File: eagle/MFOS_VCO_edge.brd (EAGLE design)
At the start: 99 x 80 mm, 110 parts, among them IC1 TL072P, IC2 LM394N, IC3 TL072P, IC4 TL072P, IC5 TL072P, IC6 TL072P, IC7 LM13700N, U1 2N5457, U2 POWER

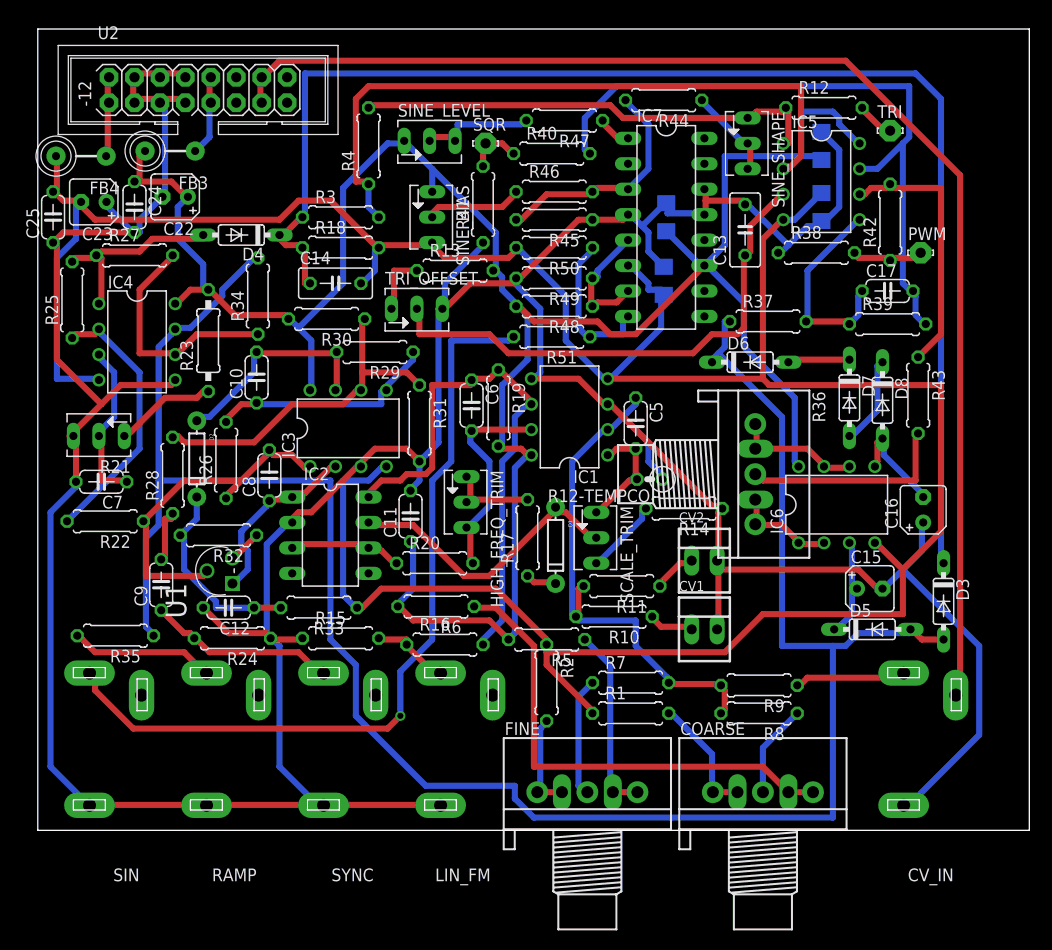
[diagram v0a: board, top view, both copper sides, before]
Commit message: flexible trimmers and grounded air outputs and connector for PWM pot
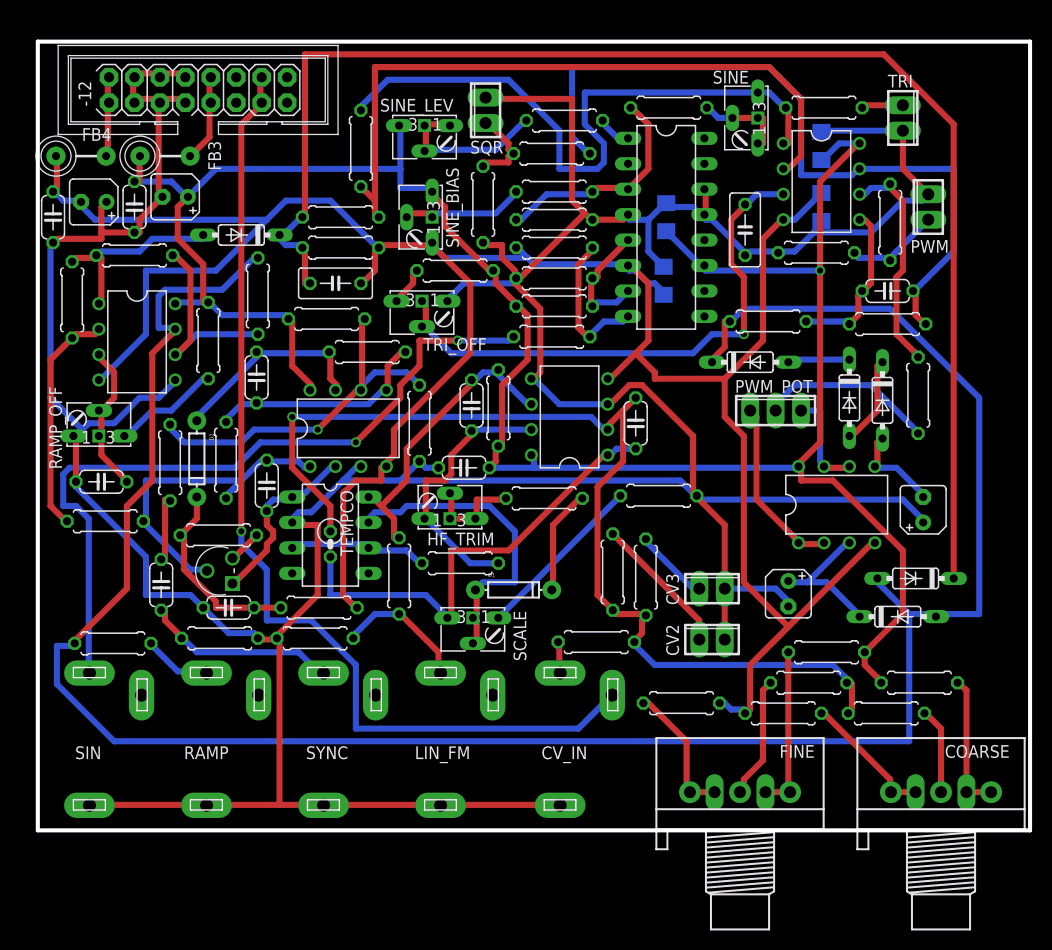
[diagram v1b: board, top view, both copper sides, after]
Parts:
- removed CV1: 22-23-2021, con-molex:22-23-2021
- removed HIGH_FREQ_TRIM, SINE_SHAPE: 100k, pot:B64Y
- removed R12-TEMPCO: 2k, rcl:0207/2V
- removed R21, TRI_OFFSET: 10k, pot:B64Y
- removed R36: 100k, pot:3RP/1610N
- removed SCALE_TRIM: 100R, pot:B64Y
- removed SINE_LEVEL: 1M, pot:B64Y
- added CV3: (no value), con-phoenix-254:2POL254
- added HF_TRIM, SINE: 100k, pot:B64W
- added PWM_POT: 100k, con-phoenix-254:3POL254
- added RAMP_OFF, TRI_OFF: 10k, pot:B64W
- added SCALE: 100R, pot:B64W
- added SINE_LEV: 1M, pot:B64W
- added TEMPCO: 2k, rcl:0207/2V
- C11: value 0.1uF -> 100n
- C8: value .005uF -> 5nF PSA
- C9: value .001uF -> 1n
- CV2: value 22-23-2021 -> (none); device con-molex:22-23-2021 -> con-phoenix-254:2POL254
- PWM, SQR, TRI: value LSP10 -> (none); device solpad:LSP10 -> con-phoenix-254:2POL254
- R23: device rcl:0207/10 -> rcl:0207/7
- SINE_BIAS: device pot:B64Y -> pot:B64W
- moved R6 48.9 mm to (88.0, 14.7)
- moved CV_IN 34.3 mm to (57.1, 0.00)
- moved R5 28.0 mm to (78.7, 17.8), turned to 0 degrees
- moved COARSE 17.8 mm to (90.2, 3.81)
- moved R7 17.8 mm to (77.0, 14.7)
- moved R9 16.8 mm to (55.8, 18.8), turned to 0 degrees
- moved FINE 15.2 mm to (70.1, 3.81)
- moved R1 15.2 mm to (74.4, 11.7)
- moved R2 13.6 mm to (64.3, 12.7), turned to 180 degrees
- moved R8 12.7 mm to (84.7, 11.7)
- moved R16 8.24 mm to (36.1, 25.4), turned to 90 degrees
- moved C15 8.14 mm to (74.9, 23.6), turned to 270 degrees
- moved CV2 7.91 mm to (67.3, 19.1)
- moved C11 7.19 mm to (42.5, 36.2), turned to 180 degrees
- moved D1 6.11 mm to (47.5, 24.0), turned to 0 degrees
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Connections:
- net +12V: now also SINE_LEV.E; no longer SINE_LEVEL.E
- net GND: now also CV3.2, PWM.2, RAMP_OFF.A, SQR.2, TRI.2, TRI_OFF.A; no longer CV1.2, R21.A, TRI_OFFSET.A
- net N$10: now also TEMPCO.1; no longer R12-TEMPCO.1
- net N$14: now also HF_TRIM.E, HF_TRIM.P$1, HF_TRIM.S; no longer HIGH_FREQ_TRIM.E, HIGH_FREQ_TRIM.S
- net N$16: now also HF_TRIM.A; no longer HIGH_FREQ_TRIM.A
- net N$18: now also CV2.1; no longer CV1.1
- net N$19: now also CV3.1; no longer CV2.1
- net N$27: now also RAMP_OFF.E; no longer R21.E
- net N$28: now also RAMP_OFF.P$1, RAMP_OFF.S; no longer R21.S
- net N$46: now also SINE.E; no longer SINE_SHAPE.E
- net N$47: now also TRI.1; no longer TRI.MP
- net N$48: now also TRI_OFF.E; no longer TRI_OFFSET.E
- net N$49: now also TRI_OFF.P$1, TRI_OFF.S; no longer TRI_OFFSET.S
- net N$52: now also PWM_POT.1; no longer R36.3, R36.6
- net N$53: now also PWM_POT.3; no longer R36.1, R36.4
- net N$54: now also PWM.1; no longer PWM.MP
- net N$57: now also SQR.1; no longer SQR.MP
- net N$59: now also PWM_POT.2; no longer R36.2
- net N$60: now also SINE.A, SINE.P$1, SINE.S; no longer SINE_SHAPE.A, SINE_SHAPE.S
- net N$62: now also SINE_BIAS.P$1
- net N$64: now also SINE_LEV.A, SINE_LEV.P$1, SINE_LEV.S; no longer SINE_LEVEL.A, SINE_LEVEL.S
- net N$7: now also SCALE.A; no longer SCALE_TRIM.A
- net N$8: now also SCALE.P$1, SCALE.S; no longer SCALE_TRIM.S
- net N$9: now also SCALE.E, TEMPCO.2; no longer R12-TEMPCO.2, SCALE_TRIM.E
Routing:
- net N$10: track 58.4 -> 104.5 mm, vias 0 -> 1
- net -12V: track 286.0 -> 250.8 mm
- net N$4: track 48.6 -> 13.8 mm
- net N$9: track 11.6 -> 46.0 mm
- net N$13: track 129.8 -> 100.2 mm, vias 0 -> 1
- net GND: track 408.6 -> 433.1 mm
- net N$40: track 54.8 -> 30.6 mm
- net N$46: track 47.0 -> 64.5 mm
- net N$35: track 209.3 -> 225.5 mm
- net N$7: track 7.59 -> 17.2 mm
- net N$18: track 4.46 -> 14.1 mm
- net N$17: track 11.3 -> 3.13 mm
- net N$36: track 14.4 -> 6.79 mm
- net N$52: track 10.3 -> 17.8 mm
- net N$15: track 3.09 -> 10.5 mm
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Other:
- board size 99 x 80 mm -> 99.1 x 78.7 mm

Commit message: slightly narrower
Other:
- board size 99.1 x 78.7 mm -> 97.8 x 78.7 mm
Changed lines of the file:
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@@
 <plain>
 <wire x1="0" y1="0" x2="0" y2="78.74" width="0.4064" layer="20"/>
-<wire x1="0" y1="78.74" x2="99.06" y2="78.74" width="0.4064" layer="20"/>
-<wire x1="99.06" y1="78.74" x2="99.06" y2="0" width="0.4064" layer="20"/>
-<wire x1="99.06" y1="0" x2="0" y2="0" width="0.4064" layer="20"/>
+<wire x1="0" y1="78.74" x2="97.79" y2="78.74" width="0.4064" layer="20"/>
+<wire x1="97.79" y1="78.74" x2="97.79" y2="0" width="0.4064" layer="20"/>
+<wire x1="97.79" y1="0" x2="0" y2="0" width="0.4064" layer="20"/>
 </plain>
 <attributes>
